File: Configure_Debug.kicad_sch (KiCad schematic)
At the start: 19 parts, among them CN5 3020-10-0300-00-TR

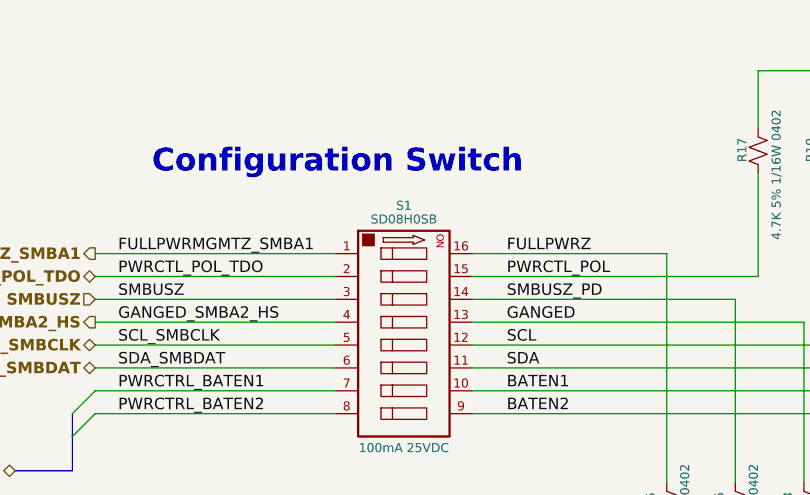
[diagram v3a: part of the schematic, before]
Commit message: 1. 完成： Configuration Switch、Configuration PinHeader 1x10、EEPROM、TUSB4020BI的布局与部分布线 2. 修改原理图TPS2561通道1和通道2的顺序以方便布局布线
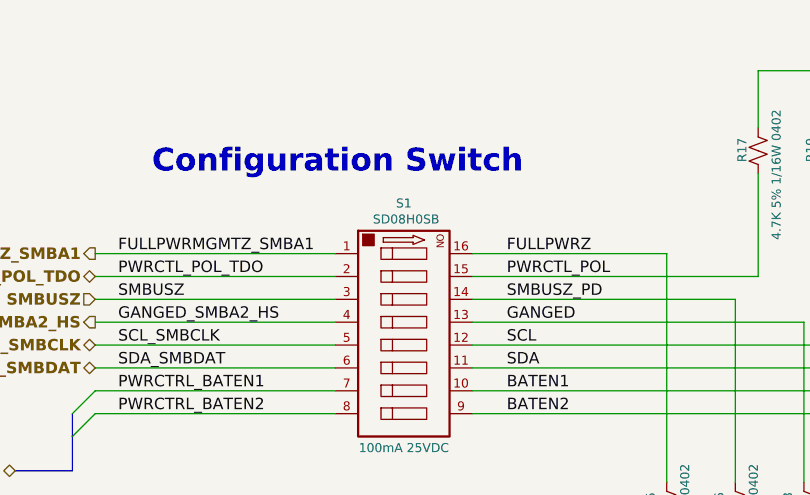
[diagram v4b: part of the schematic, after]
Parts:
- removed S1: 100mA 25VDC, MY_Switch:CK_SW_SD08H0SB, symbol MY_Switch:SD08H0SB
- added S1: 100mA 25VDC, MY_Switch:CK_SW_SD08H0SB, symbol MY_SW:SD08H0SB
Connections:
- net BATEN1: now also S1.10
- net BATEN2: now also S1.9
- net FULLPWRMGMTZ_SMBA1: now also S1.1
- net FULLPWRZ: now also S1.16
- net GANGED: now also S1.13
- net GANGED_SMBA2_HS: now also S1.4
- net PWRCTL_POL: now also S1.15
- net PWRCTL_POL_TDO: now also S1.2
- net PWRCTRL_BATEN1: now also S1.7
- net PWRCTRL_BATEN2: now also S1.8
- net SCL: now also S1.12
- net SCL_SMBCLK: now also S1.5
- net SDA: now also S1.11
- net SDA_SMBDAT: now also S1.6
- net SMBUSZ: now also S1.3
- net SMBUSZ_PD: now also S1.14
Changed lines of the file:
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@@
+	)
+	(symbol
+		(lib_id "MY_SW:SD08H0SB")
+		(at 83.82 53.34 0)
+		(unit 1)
+		(exclude_from_sim no)
+		(in_bom yes)
+		(on_board yes)
+		(dnp no)
+		(property "Reference" "S1"
+			(at 83.82 37.592 0)
+			(effects
+				(font
+					(size 1 1)
+				)
+			)
+		)
+		(property "Value" "100mA 25VDC"
+			(at 83.82 64.77 0)
+			(effects
+				(font
+					(size 1 1)
+				)
+			)
+		)
+		(property "Footprint" "MY_Switch:CK_SW_SD08H0SB"
+			(at 83.82 68.072 0)
+			(effects
+				(font
+					(size 1.27 1.27)
+				)
+				(justify bottom)
+				(hide yes)
+			)
+		)
+		(property "Datasheet" "kicad-embed://SD08H0SBR.pdf"
+			(at 83.82 78.74 0)
+			(effects
+				(font
+					(size 1.27 1.27)
+				)
+				(hide yes)
+			)
+		)
+		(property "Description" "拨码开关x8 SMD 100mA 25VDC"
+			(at 83.82 76.708 0)
+			(effects
+				(font
+					(size 1.27 1.27)
+				)
+				(hide yes)
+			)
+		)
+		(property "MPN" "SD08H0SB"
+			(at 84.074 39.37 0)
+			(effects
+				(font
+					(size 1 1)
+				)
+			)
+		)
+		(property "Manufacturer" "C&K"
+			(at 83.82 74.676 0)
+			(effects
+				(font
+					(size 1.27 1.27)
+				)
+				(hide yes)
+			)
+		)
+		(property "详细描述" "DIP 开关 SPST 8 位置 表面贴装型 滑动式（标准） 触动器 100mA 25VDC"
+			(at 83.82 81.28 0)
+			(effects
+				(font
+					(size 1.27 1.27)
+				)
+				(hide yes)
+			)
+		)
+		(pin "3"
+		)
+		(pin "9"
+		)
+		(pin "6"
+		)
+		(pin "7"
+		)
+		(pin "5"
+		)
+		(pin "11"
+		)
+		(pin "10"
+		)
+		(pin "1"
+		)
+		(pin "4"
+		)
+		(pin "8"
+		)
+		(pin "13"
+		)
+		(pin "14"
+		)
+		(pin "15"
+		)
+		(pin "16"
+		)
+		(pin "2"
+		)
+		(pin "12"
+		)
+		(instances
+			(project "USBHub"
+				(path "/07e28d9d-adcb-473d-a362-1ef0c979820d/150922e4-fdd8-4f23-80c4-730d3fbf126a"
+					(reference "S1")
+					(unit 1)
+				)
+			)
+		)
 	)
 	(symbol
@@
 					(unit 1)
 				)
-			)
-		)
-	)
-	(symbol
-		(lib_id "MY_Switch:SD08H0SB")
-		(at 83.82 53.34 0)
-		(unit 1)
-		(exclude_from_sim no)
-		(in_bom yes)
-		(on_board yes)
-		(dnp no)
-		(property "Reference" "S1"
-			(at 83.82 37.846 0)
-			(effects
-				(font
-					(size 1 1)
-				)
-			)
-		)
-		(property "Value" "100mA 25VDC"
-			(at 83.82 64.77 0)
-			(effects
-				(font
-					(size 1 1)
-				)
-			)
-		)
-		(property "Footprint" "MY_Switch:CK_SW_SD08H0SB"
-			(at 83.82 68.072 0)
-			(effects
-				(font
-					(size 1.27 1.27)
-				)
-				(justify bottom)
-				(hide yes)
-			)
-		)
-		(property "Datasheet" "kicad-embed://SD08H0SBR.pdf"
-			(at 83.82 78.74 0)
-			(effects
-				(font
-					(size 1.27 1.27)
-				)
-				(hide yes)
-			)
-		)
-		(property "Description" "拨码开关x8 SMD 100mA 25VDC"
-			(at 83.82 76.708 0)
-			(effects
-				(font
-					(size 1.27 1.27)
-				)
-				(hide yes)
-			)
-		)
-		(property "MPN" "SD08H0SB"
-			(at 83.82 39.37 0)
-			(effects
-				(font
-					(size 1 1)
-				)
-			)
-		)
-		(property "Manufacturer" "C&K"
-			(at 83.82 74.676 0)
-			(effects
-				(font
-					(size 1.27 1.27)
-				)
-				(hide yes)
-			)
-		)
-		(property "详细描述" "DIP 开关 SPST 8 位置 表面贴装型 滑动式（标准） 触动器 100mA 25VDC"
-			(at 83.82 81.28 0)
-			(effects
-				(font
-					(size 1.27 1.27)
-				)
-				(hide yes)
-			)
-		)
-		(pin "5"
-		)
-		(pin "6"
-		)
-		(pin "16"
-		)
-		(pin "12"
-		)
-		(pin "3"
-		)
-		(pin "1"
-		)
-		(pin "2"
-		)
-		(pin "4"
-		)
-		(pin "7"
-		)
-		(pin "8"
-		)
-		(pin "15"
-		)
-		(pin "14"
-		)
-		(pin "13"
-		)
-		(pin "10"
-		)
-		(pin "9"
-		)
-		(pin "11"
-		)
-		(instances
-			(project ""
-				(path "/07e28d9d-adcb-473d-a362-1ef0c979820d/150922e4-fdd8-4f23-80c4-730d3fbf126a"
-					(reference "S1")
-					(unit 1)
-				)
